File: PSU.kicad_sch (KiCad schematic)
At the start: 11 parts, among them J1 Mini USB Female, J2 Battery Connector, U3 AMS1117-3.3

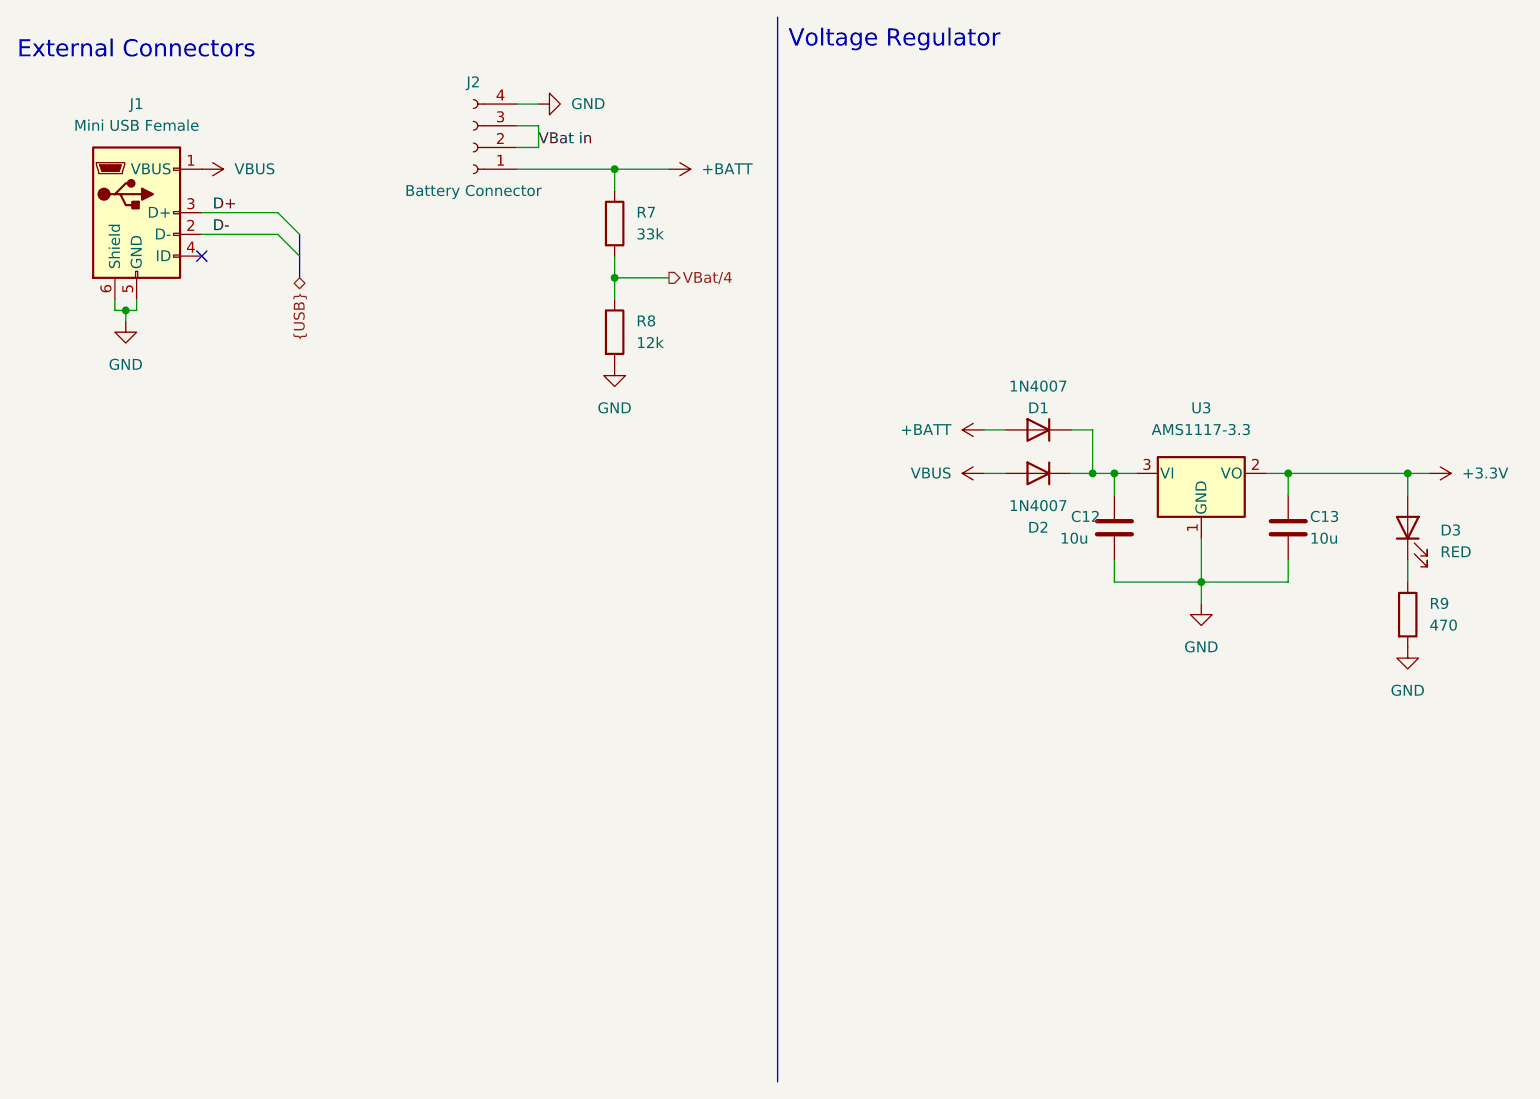
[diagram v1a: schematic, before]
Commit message: Geographical reannotated
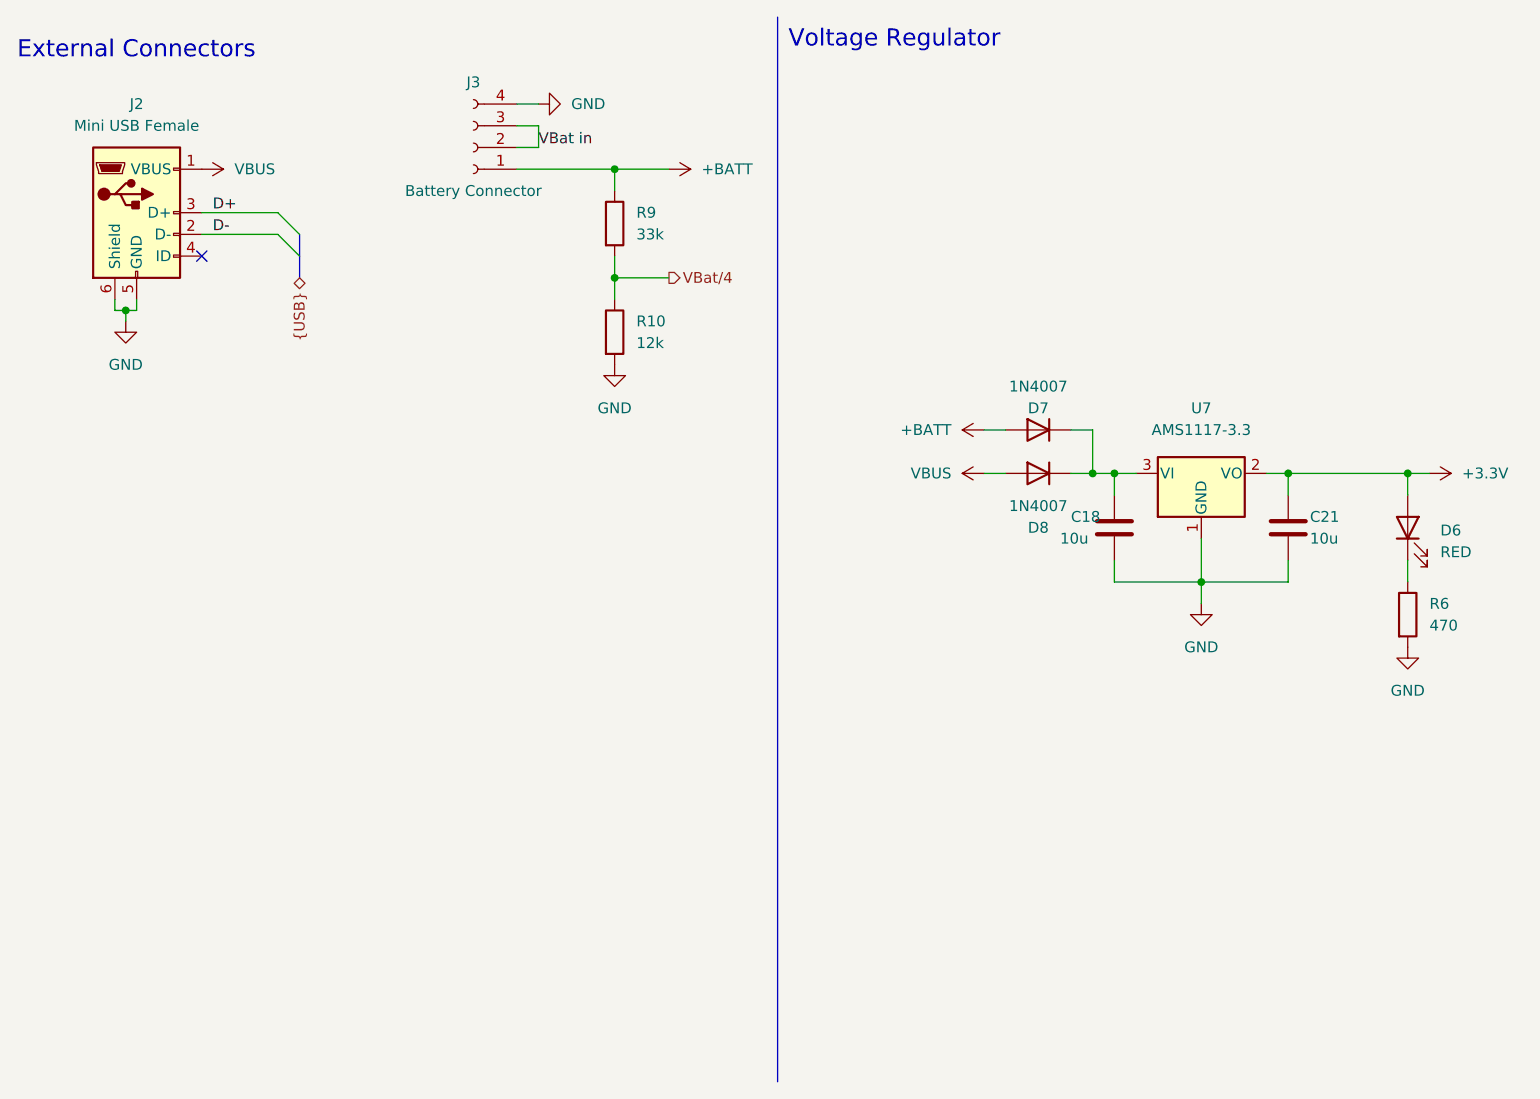
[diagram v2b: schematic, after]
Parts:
- renumbered C12 to C18, C13 to C21, D3 to D6, D1 to D7, D2 to D8, J1 to J2, J2 to J3, R8 to R10, R9 to R6, R7 to R9, U3 to U7
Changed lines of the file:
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@@
   (symbol (lib_id "Device:LED") (at 175.26 71.12 90) (unit 1)
     (in_bom yes) (on_board yes) (fields_autoplaced)
-    (property "Reference" "D3" (id 0) (at 179.07 71.4374 90)
+    (property "Reference" "D6" (id 0) (at 179.07 71.4374 90)
       (effects (font (size 1.27 1.27)) (justify right))
     )
@@
   (symbol (lib_id "Device:R") (at 82.55 35.56 0) (unit 1)
     (in_bom yes) (on_board yes) (fields_autoplaced)
-    (property "Reference" "R7" (id 0) (at 85.09 34.2899 0)
+    (property "Reference" "R9" (id 0) (at 85.09 34.2899 0)
       (effects (font (size 1.27 1.27)) (justify left))
     )
@@
   (symbol (lib_id "Device:C") (at 140.97 71.12 0) (mirror y) (unit 1)
     (in_bom yes) (on_board yes)
-    (property "Reference" "C12" (id 0) (at 135.89 69.85 0)
+    (property "Reference" "C18" (id 0) (at 135.89 69.85 0)
       (effects (font (size 1.27 1.27)) (justify right))
     )
@@
   (symbol (lib_id "Connector:Conn_01x04_Female") (at 66.04 26.67 180) (unit 1)
     (in_bom yes) (on_board yes)
-    (property "Reference" "J2" (id 0) (at 66.04 19.05 0))
+    (property "Reference" "J3" (id 0) (at 66.04 19.05 0))
     (property "Value" "Battery Connector" (id 1) (at 66.04 31.75 0))
     (property "Footprint" "YAR_Connectors:ScrewTerm_2.54x04" (id 2) (at 66.04 26.67 0)
@@
   (symbol (lib_id "Device:C") (at 161.29 71.12 0) (mirror y) (unit 1)
     (in_bom yes) (on_board yes)
-    (property "Reference" "C13" (id 0) (at 163.83 69.85 0)
+    (property "Reference" "C21" (id 0) (at 163.83 69.85 0)
       (effects (font (size 1.27 1.27)) (justify right))
     )
@@
   (symbol (lib_id "Device:R") (at 82.55 48.26 0) (unit 1)
     (in_bom yes) (on_board yes) (fields_autoplaced)
-    (property "Reference" "R8" (id 0) (at 85.09 46.9899 0)
+    (property "Reference" "R10" (id 0) (at 85.09 46.9899 0)
       (effects (font (size 1.27 1.27)) (justify left))
     )
@@
   (symbol (lib_id "Device:R") (at 175.26 81.28 0) (unit 1)
     (in_bom yes) (on_board yes) (fields_autoplaced)
-    (property "Reference" "R9" (id 0) (at 177.8 80.0099 0)
+    (property "Reference" "R6" (id 0) (at 177.8 80.0099 0)
       (effects (font (size 1.27 1.27)) (justify left))
     )
@@
   (symbol (lib_id "Connector:USB_OTG") (at 26.67 34.29 0) (unit 1)
     (in_bom yes) (on_board yes) (fields_autoplaced)
-    (property "Reference" "J1" (id 0) (at 26.67 21.59 0))
+    (property "Reference" "J2" (id 0) (at 26.67 21.59 0))
     (property "Value" "Mini USB Female" (id 1) (at 26.67 24.13 0))
     (property "Footprint" "Connector_USB:USB_Mini-B_Lumberg_2486_01_Horizontal" (id 2) (at 30.48 35.56 0)
@@
   (symbol (lib_id "Diode:1N914") (at 132.08 64.77 0) (mirror y) (unit 1)
     (in_bom yes) (on_board yes) (fields_autoplaced)
-    (property "Reference" "D2" (id 0) (at 132.08 71.12 0))
+    (property "Reference" "D8" (id 0) (at 132.08 71.12 0))
     (property "Value" "1N4007" (id 1) (at 132.08 68.58 0))
     (property "Footprint" "Diode_SMD:D_SOD-123" (id 2) (at 132.08 69.215 0)
@@
   (symbol (lib_id "Diode:1N914") (at 132.08 59.69 0) (mirror y) (unit 1)
     (in_bom yes) (on_board yes)
-    (property "Reference" "D1" (id 0) (at 132.08 57.15 0))
+    (property "Reference" "D7" (id 0) (at 132.08 57.15 0))
     (property "Value" "1N4007" (id 1) (at 132.08 54.61 0))
     (property "Footprint" "Diode_SMD:D_SOD-123" (id 2) (at 132.08 64.135 0)
@@
   (symbol (lib_id "Regulator_Linear:NCP1117-3.3_SOT223") (at 151.13 64.77 0) (unit 1)
     (in_bom yes) (on_board yes) (fields_autoplaced)
-    (property "Reference" "U3" (id 0) (at 151.13 57.15 0))
+    (property "Reference" "U7" (id 0) (at 151.13 57.15 0))
     (property "Value" "AMS1117-3.3" (id 1) (at 151.13 59.69 0))
     (property "Footprint" "Package_TO_SOT_SMD:SOT-223-3_TabPin2" (id 2) (at 151.13 59.69 0)

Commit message: Final refinements before issue to JLC
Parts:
- renumbered C18 to C12, C21 to C13, D7 to D1, D8 to D2, D6 to D3, R9 to R7, R10 to R8, R6 to R9, U7 to U3
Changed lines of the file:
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@@
   (symbol (lib_id "power:+3.3V") (at 177.8 64.77 270) (unit 1)
     (in_bom yes) (on_board yes) (fields_autoplaced)
-    (property "Reference" "#PWR029" (id 0) (at 173.99 64.77 0)
+    (property "Reference" "#PWR031" (id 0) (at 173.99 64.77 0)
       (effects (font (size 1.27 1.27)) hide)
     )
@@
   (symbol (lib_id "Device:LED") (at 175.26 71.12 90) (unit 1)
     (in_bom yes) (on_board yes) (fields_autoplaced)
-    (property "Reference" "D6" (id 0) (at 179.07 71.4374 90)
+    (property "Reference" "D3" (id 0) (at 179.07 71.4374 90)
       (effects (font (size 1.27 1.27)) (justify right))
     )
@@
   (symbol (lib_id "Device:R") (at 82.55 35.56 0) (unit 1)
     (in_bom yes) (on_board yes) (fields_autoplaced)
-    (property "Reference" "R9" (id 0) (at 85.09 34.2899 0)
+    (property "Reference" "R7" (id 0) (at 85.09 34.2899 0)
       (effects (font (size 1.27 1.27)) (justify left))
     )
@@
   (symbol (lib_id "Device:C") (at 140.97 71.12 0) (mirror y) (unit 1)
     (in_bom yes) (on_board yes)
-    (property "Reference" "C18" (id 0) (at 135.89 69.85 0)
+    (property "Reference" "C12" (id 0) (at 135.89 69.85 0)
       (effects (font (size 1.27 1.27)) (justify right))
     )
@@
   (symbol (lib_id "power:+BATT") (at 88.9 29.21 270) (unit 1)
     (in_bom yes) (on_board yes) (fields_autoplaced)
-    (property "Reference" "#PWR024" (id 0) (at 85.09 29.21 0)
+    (property "Reference" "#PWR026" (id 0) (at 85.09 29.21 0)
       (effects (font (size 1.27 1.27)) hide)
     )
@@
   (symbol (lib_id "Device:C") (at 161.29 71.12 0) (mirror y) (unit 1)
     (in_bom yes) (on_board yes)
-    (property "Reference" "C21" (id 0) (at 163.83 69.85 0)
+    (property "Reference" "C13" (id 0) (at 163.83 69.85 0)
       (effects (font (size 1.27 1.27)) (justify right))
     )
@@
   (symbol (lib_id "power:GND") (at 175.26 85.09 0) (unit 1)
     (in_bom yes) (on_board yes) (fields_autoplaced)
-    (property "Reference" "#PWR028" (id 0) (at 175.26 91.44 0)
+    (property "Reference" "#PWR030" (id 0) (at 175.26 91.44 0)
       (effects (font (size 1.27 1.27)) hide)
     )
@@
   (symbol (lib_id "power:GND") (at 25.4 46.99 0) (unit 1)
     (in_bom yes) (on_board yes) (fields_autoplaced)
-    (property "Reference" "#PWR020" (id 0) (at 25.4 53.34 0)
+    (property "Reference" "#PWR022" (id 0) (at 25.4 53.34 0)
       (effects (font (size 1.27 1.27)) hide)
     )
@@
   (symbol (lib_id "power:VBUS") (at 34.29 29.21 270) (unit 1)
     (in_bom yes) (on_board yes) (fields_autoplaced)
-    (property "Reference" "#PWR021" (id 0) (at 30.48 29.21 0)
+    (property "Reference" "#PWR023" (id 0) (at 30.48 29.21 0)
       (effects (font (size 1.27 1.27)) hide)
     )
@@
   (symbol (lib_id "Device:R") (at 82.55 48.26 0) (unit 1)
     (in_bom yes) (on_board yes) (fields_autoplaced)
-    (property "Reference" "R10" (id 0) (at 85.09 46.9899 0)
+    (property "Reference" "R8" (id 0) (at 85.09 46.9899 0)
       (effects (font (size 1.27 1.27)) (justify left))
     )
@@
   (symbol (lib_id "Device:R") (at 175.26 81.28 0) (unit 1)
     (in_bom yes) (on_board yes) (fields_autoplaced)
-    (property "Reference" "R6" (id 0) (at 177.8 80.0099 0)
+    (property "Reference" "R9" (id 0) (at 177.8 80.0099 0)
       (effects (font (size 1.27 1.27)) (justify left))
     )
@@
   (symbol (lib_id "power:GND") (at 82.55 52.07 0) (unit 1)
     (in_bom yes) (on_board yes) (fields_autoplaced)
-    (property "Reference" "#PWR023" (id 0) (at 82.55 58.42 0)
+    (property "Reference" "#PWR025" (id 0) (at 82.55 58.42 0)
       (effects (font (size 1.27 1.27)) hide)
     )
@@
   (symbol (lib_id "Diode:1N914") (at 132.08 64.77 0) (mirror y) (unit 1)
     (in_bom yes) (on_board yes) (fields_autoplaced)
-    (property "Reference" "D8" (id 0) (at 132.08 71.12 0))
+    (property "Reference" "D2" (id 0) (at 132.08 71.12 0))
     (property "Value" "1N4007" (id 1) (at 132.08 68.58 0))
     (property "Footprint" "Diode_SMD:D_SOD-123" (id 2) (at 132.08 69.215 0)
@@
   (symbol (lib_id "Diode:1N914") (at 132.08 59.69 0) (mirror y) (unit 1)
     (in_bom yes) (on_board yes)
-    (property "Reference" "D7" (id 0) (at 132.08 57.15 0))
+    (property "Reference" "D1" (id 0) (at 132.08 57.15 0))
     (property "Value" "1N4007" (id 1) (at 132.08 54.61 0))
     (property "Footprint" "Diode_SMD:D_SOD-123" (id 2) (at 132.08 64.135 0)
@@
   (symbol (lib_id "power:VBUS") (at 125.73 64.77 90) (mirror x) (unit 1)
     (in_bom yes) (on_board yes) (fields_autoplaced)
-    (property "Reference" "#PWR026" (id 0) (at 129.54 64.77 0)
+    (property "Reference" "#PWR028" (id 0) (at 129.54 64.77 0)
       (effects (font (size 1.27 1.27)) hide)
     )
@@
   (symbol (lib_id "power:GND") (at 151.13 80.01 0) (unit 1)
     (in_bom yes) (on_board yes) (fields_autoplaced)
-    (property "Reference" "#PWR027" (id 0) (at 151.13 86.36 0)
+    (property "Reference" "#PWR029" (id 0) (at 151.13 86.36 0)
       (effects (font (size 1.27 1.27)) hide)
     )
@@
   (symbol (lib_id "power:GND") (at 73.66 21.59 90) (unit 1)
     (in_bom yes) (on_board yes) (fields_autoplaced)
-    (property "Reference" "#PWR022" (id 0) (at 80.01 21.59 0)
+    (property "Reference" "#PWR024" (id 0) (at 80.01 21.59 0)
       (effects (font (size 1.27 1.27)) hide)
     )
@@
   (symbol (lib_id "power:+BATT") (at 125.73 59.69 90) (mirror x) (unit 1)
     (in_bom yes) (on_board yes) (fields_autoplaced)
-    (property "Reference" "#PWR025" (id 0) (at 129.54 59.69 0)
+    (property "Reference" "#PWR027" (id 0) (at 129.54 59.69 0)
       (effects (font (size 1.27 1.27)) hide)
     )
@@
   (symbol (lib_id "Regulator_Linear:NCP1117-3.3_SOT223") (at 151.13 64.77 0) (unit 1)
     (in_bom yes) (on_board yes) (fields_autoplaced)
-    (property "Reference" "U7" (id 0) (at 151.13 57.15 0))
+    (property "Reference" "U3" (id 0) (at 151.13 57.15 0))
     (property "Value" "AMS1117-3.3" (id 1) (at 151.13 59.69 0))
     (property "Footprint" "Package_TO_SOT_SMD:SOT-223-3_TabPin2" (id 2) (at 151.13 59.69 0)

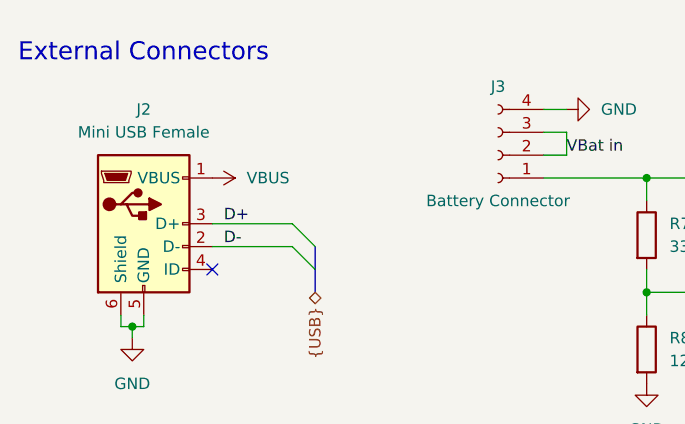
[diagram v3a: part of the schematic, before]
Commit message: rev2 changes excluding pyro
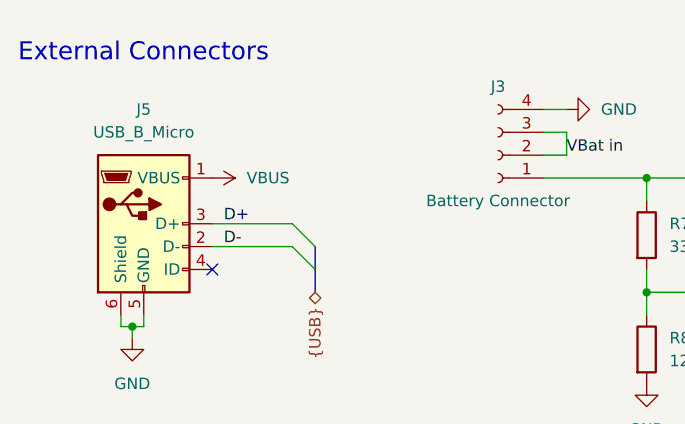
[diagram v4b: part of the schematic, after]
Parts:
- removed J2: Mini USB Female, Connector_USB:USB_Mini-B_Lumberg_2486_01_Horizontal, symbol Connector:USB_OTG
- added J5: USB_B_Micro, YAR_Connectors:USB-micro-b-molex-0476420001, symbol Connector:USB_B_Micro
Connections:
- net D+: now also J5.3 (D+)
- net D-: now also J5.2 (D-)
- net GND: now also J5.5 (GND), J5.6 (Shield)
- net VBUS: now also J5.1 (VBUS)
